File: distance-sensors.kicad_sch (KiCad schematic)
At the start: 5 parts, among them J12 Conn_01x05, J13 Conn_01x05, J14 Conn_01x05, J15 Conn_01x05, J16 Conn_01x05

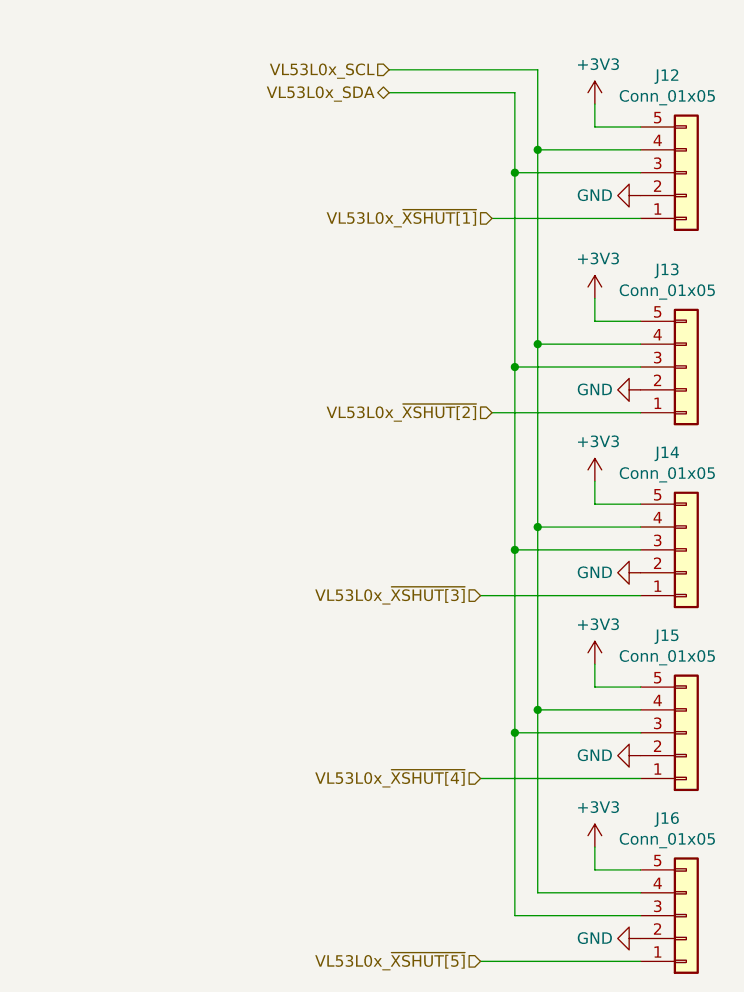
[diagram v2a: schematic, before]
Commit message: Cleanup distance sensors schematic
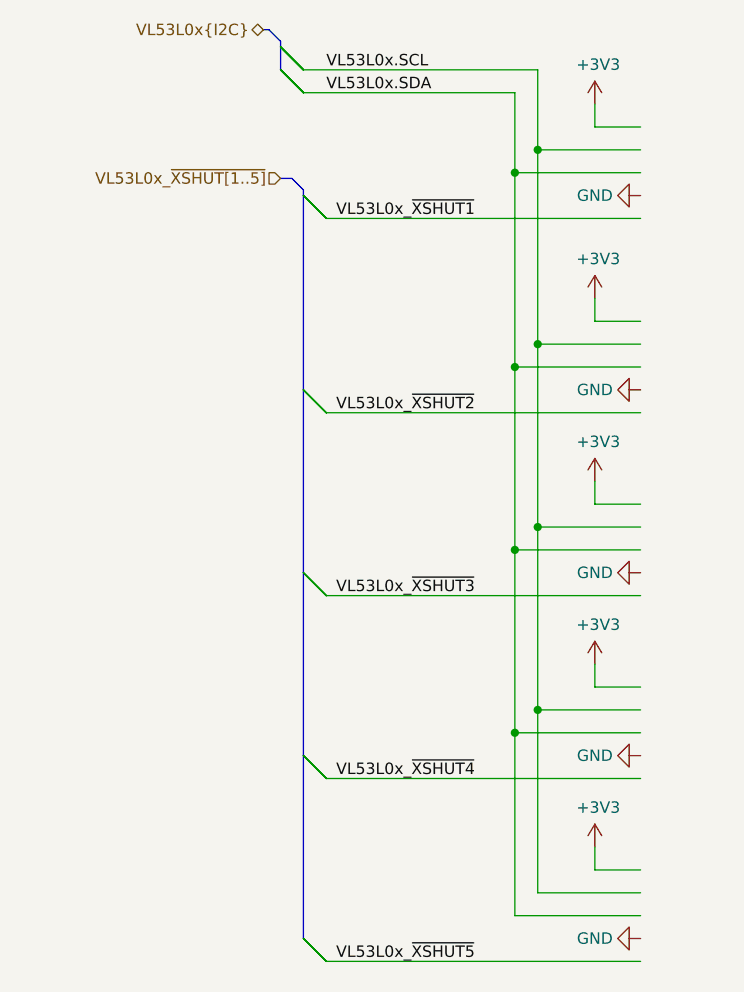
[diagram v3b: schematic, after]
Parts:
- removed J12, J13, J14, J15, J16: Conn_01x05, connector_brd2brd:01x05_1.0x0.5mm_SMD, symbol Connector_Generic:Conn_01x05

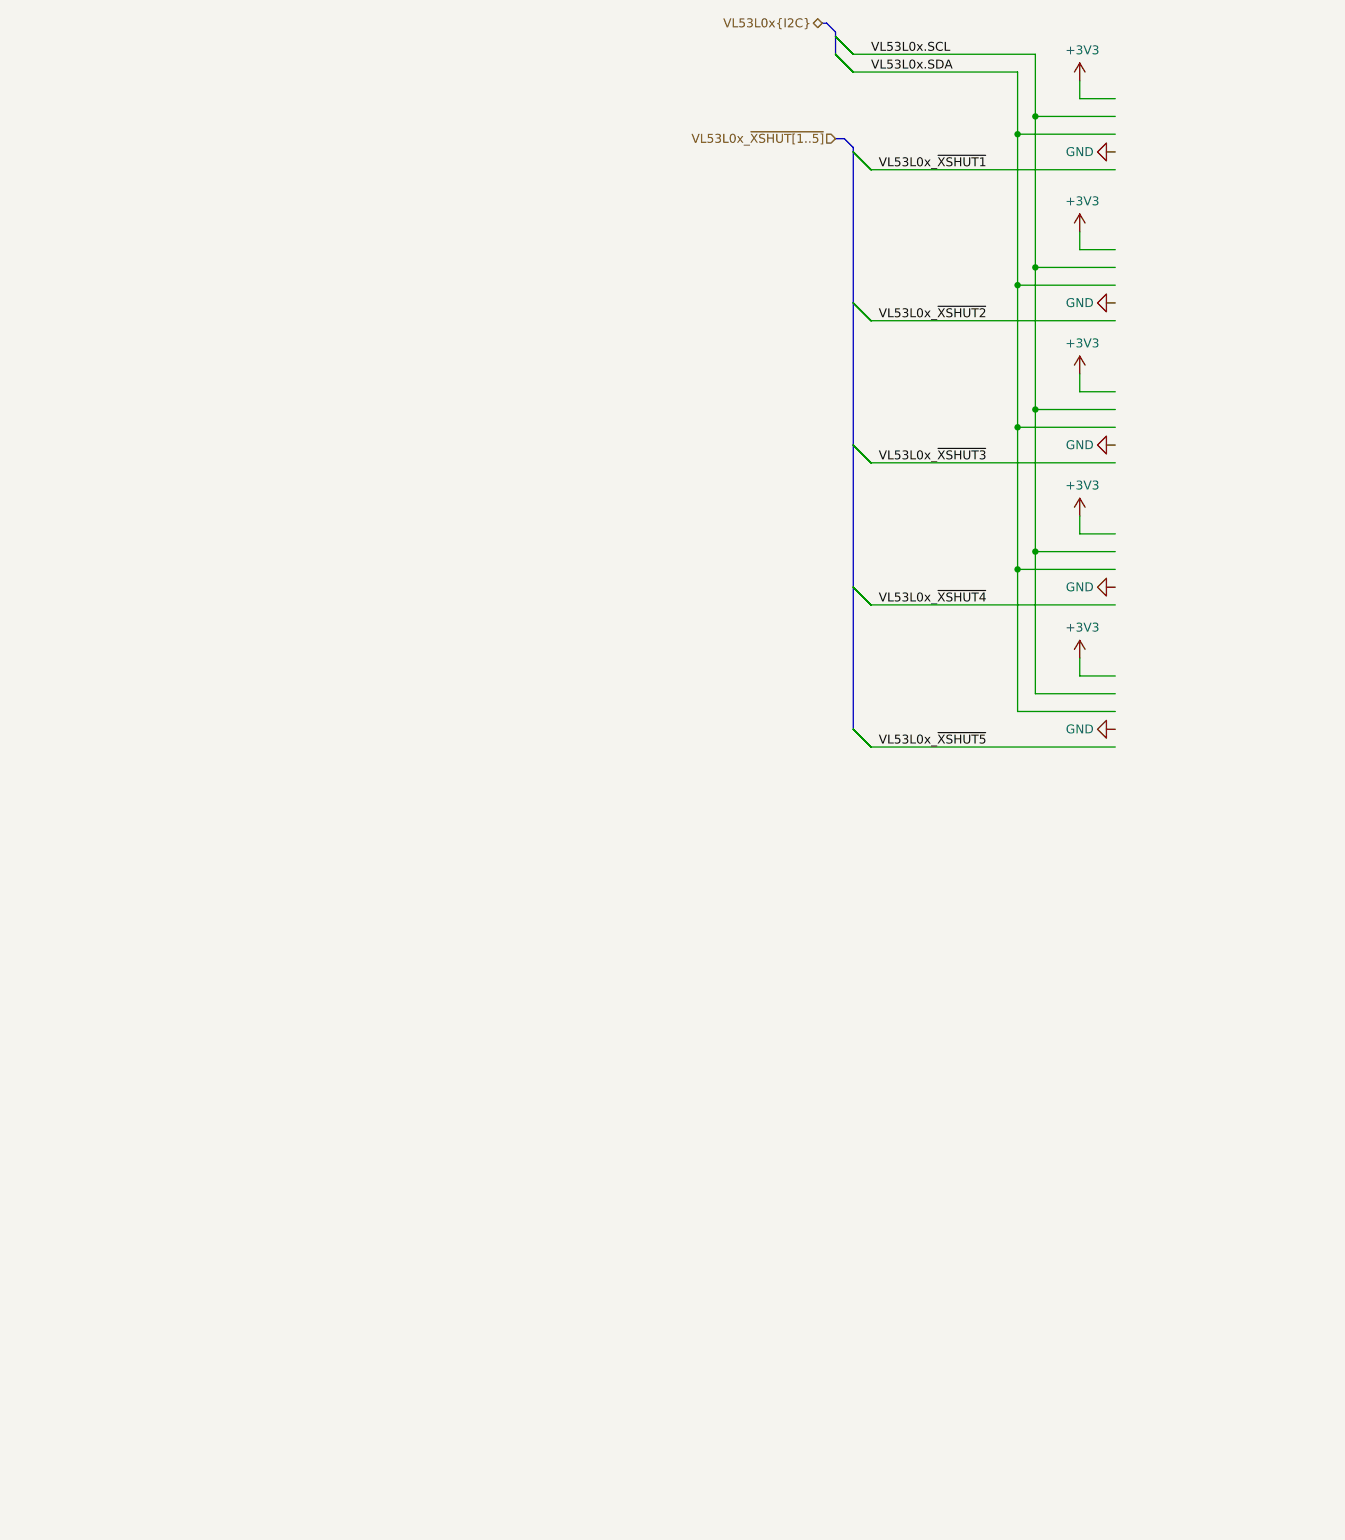
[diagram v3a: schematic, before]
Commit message: Add led driving fets
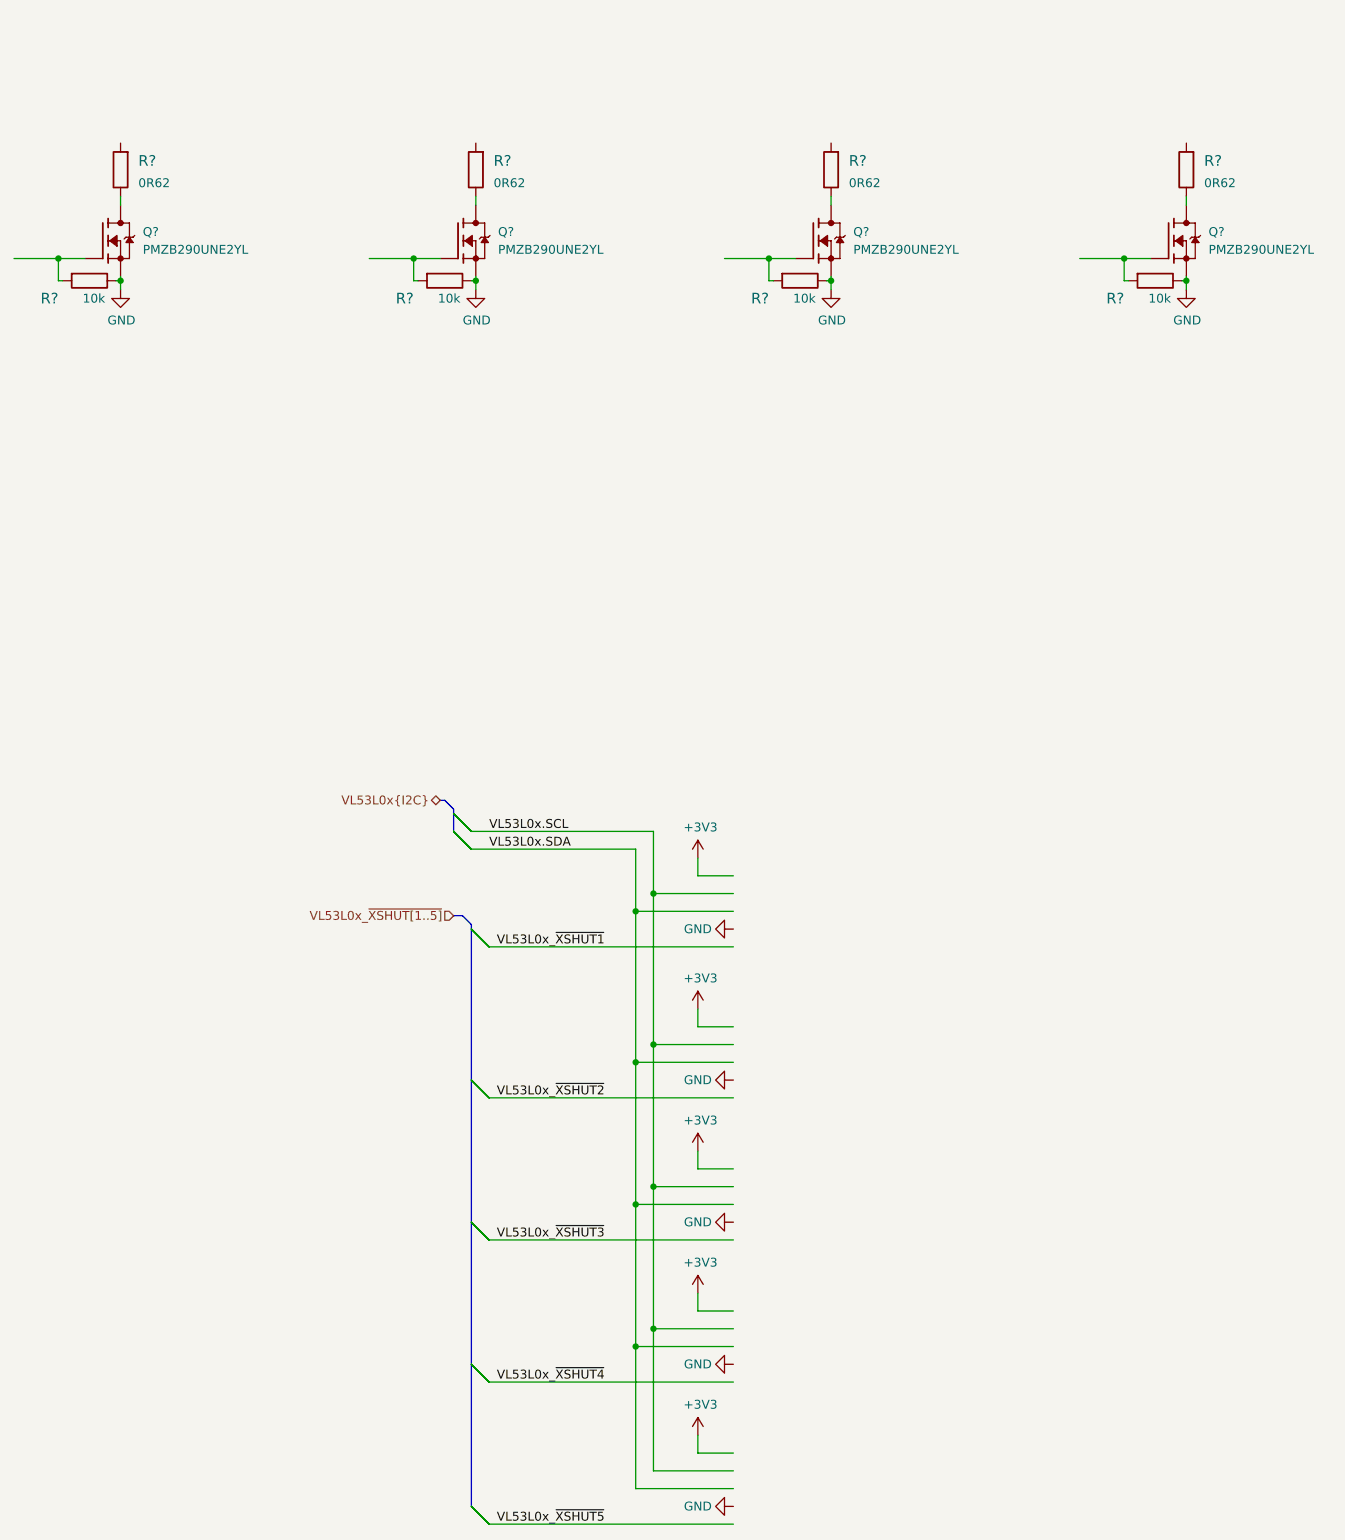
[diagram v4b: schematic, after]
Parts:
- added Q? (x4): PMZB290UNE2YL, antmicro-footprints:SOT-883, symbol antmicroTransistorsFETsMOSFETsSingle:PMZB290UNE2YL
- added R? (x4): R_10k_0402, antmicro-footprints:0402-res, symbol antmicroResistors0402:R_10k_0402
- added R? (x4): R_0R62_0603, antmicro-footprints:0603-res, symbol antmicroResistors0603:R_0R62_0603
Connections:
- net GND: now also Q?.2 (S), Q?.2 (S), Q?.2 (S), Q?.2 (S), R?.1, R?.1, R?.1, R?.1
- new net: Q?.1 (G), R?.2 (x4)
- new net: Q?.3 (D), R?.1 (x4)

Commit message: Remove VLX wiring
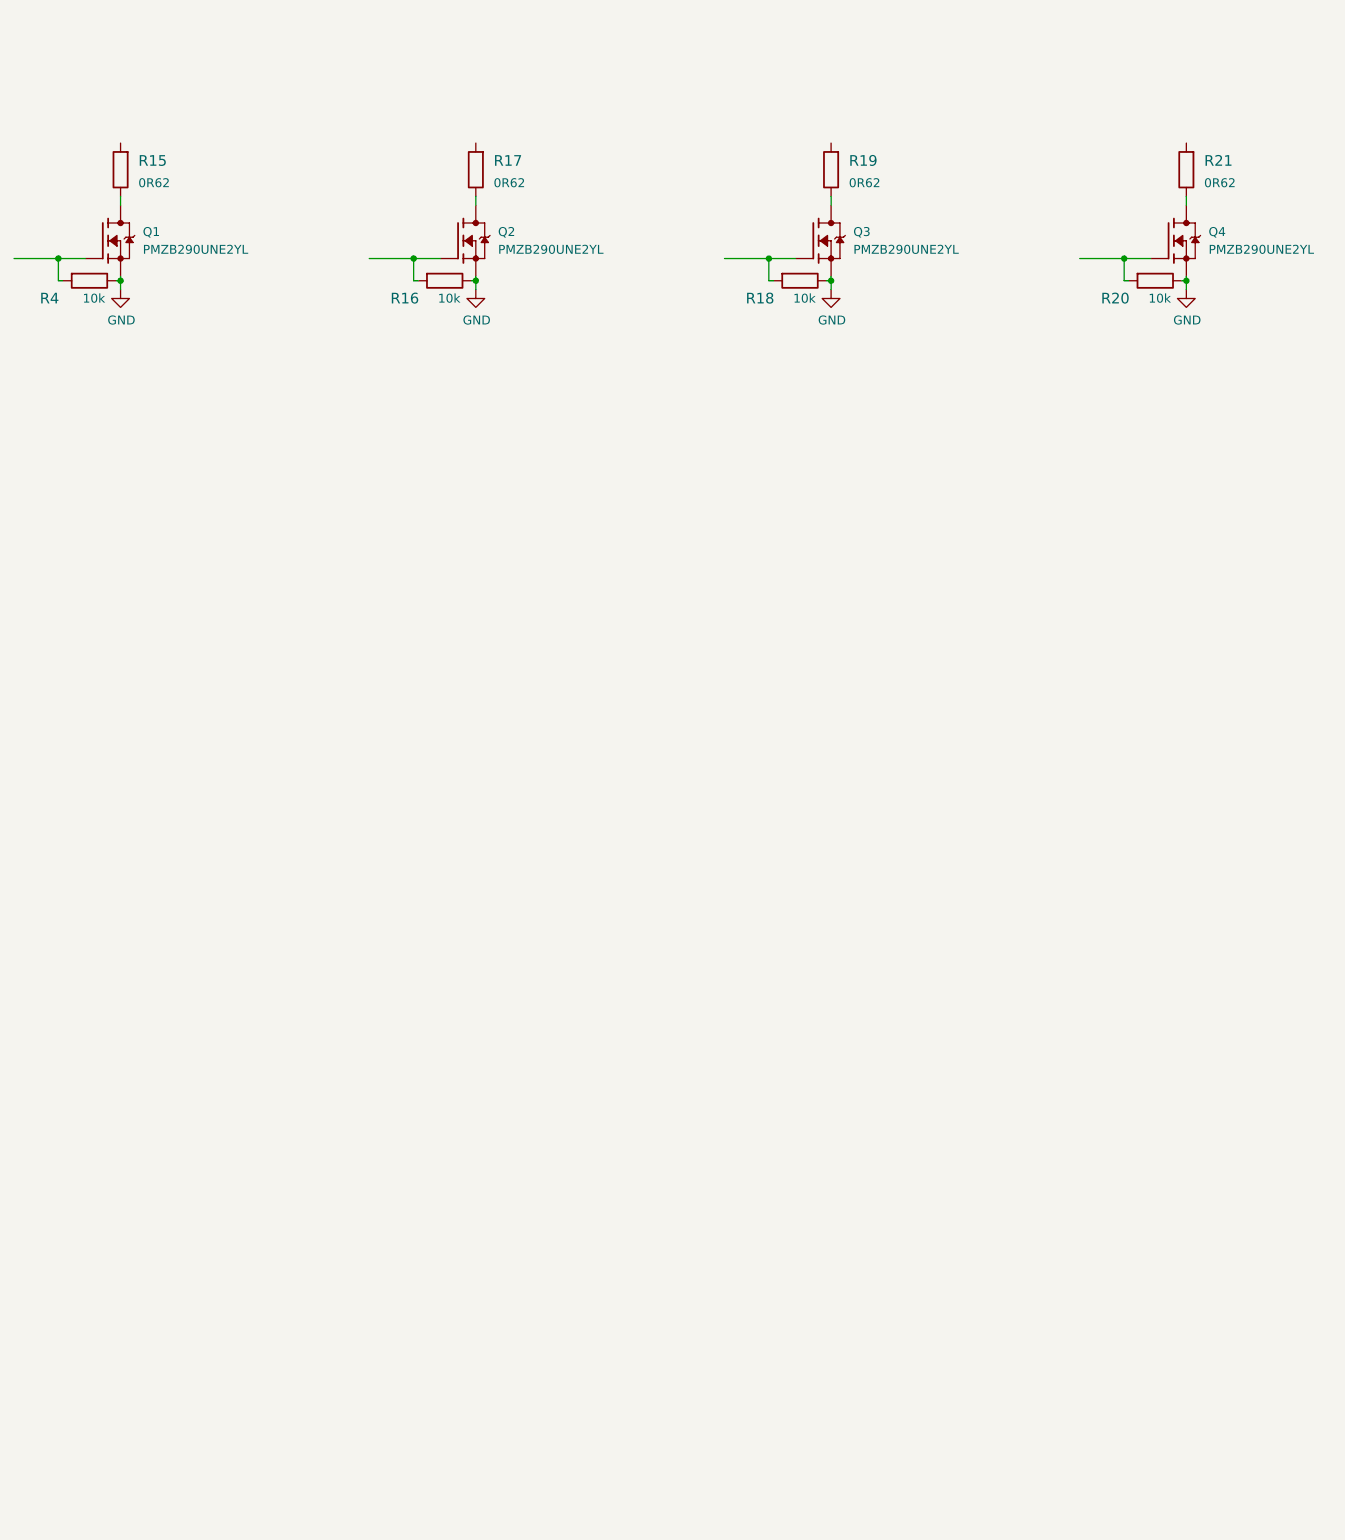
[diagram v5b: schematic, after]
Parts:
- gave numbers to parts that had none: 12

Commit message: Loclib, cleanup
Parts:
- Q1, Q2, Q3, Q4: footprint antmicro-footprints:SOT-883 -> synermycha-electronics-footprints:SOT-883; symbol antmicroTransistorsFETsMOSFETsSingle:PMZB290UNE2YL -> synermycha-electronics:PMZB290UNE2YL
- R15, R17, R19, R21: footprint antmicro-footprints:0603-res -> synermycha-electronics-footprints:0603-res; symbol antmicroResistors0603:R_0R62_0603 -> synermycha-electronics:R_0R62_0603
- R16, R18, R20, R4: footprint antmicro-footprints:0402-res -> synermycha-electronics-footprints:0402-res; symbol antmicroResistors0402:R_10k_0402 -> synermycha-electronics:R_10k_0402
